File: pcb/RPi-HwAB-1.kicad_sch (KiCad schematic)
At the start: 5 parts, among them U1 CAT24C256

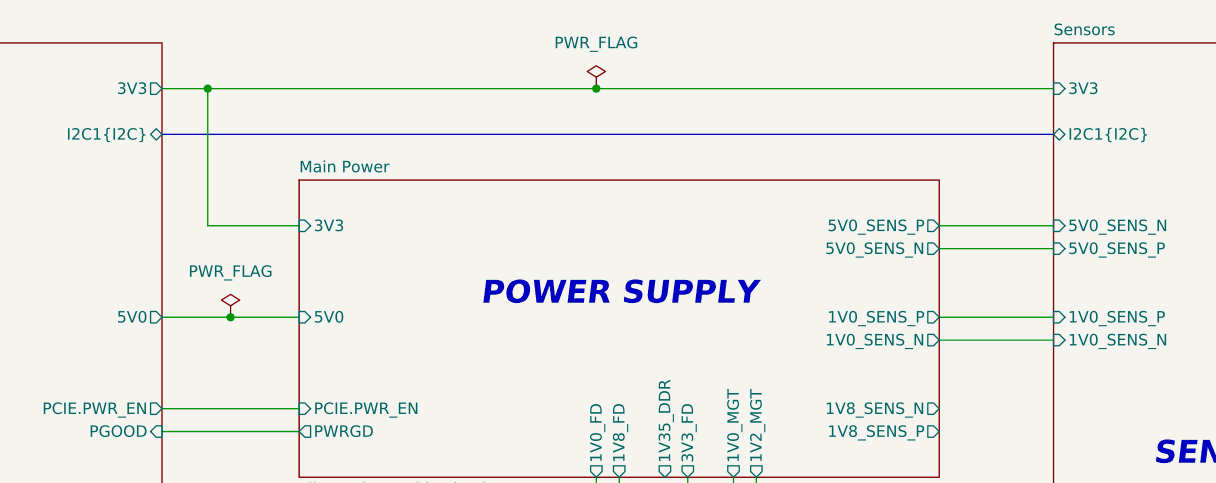
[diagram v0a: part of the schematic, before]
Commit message: moved stuff around, bom
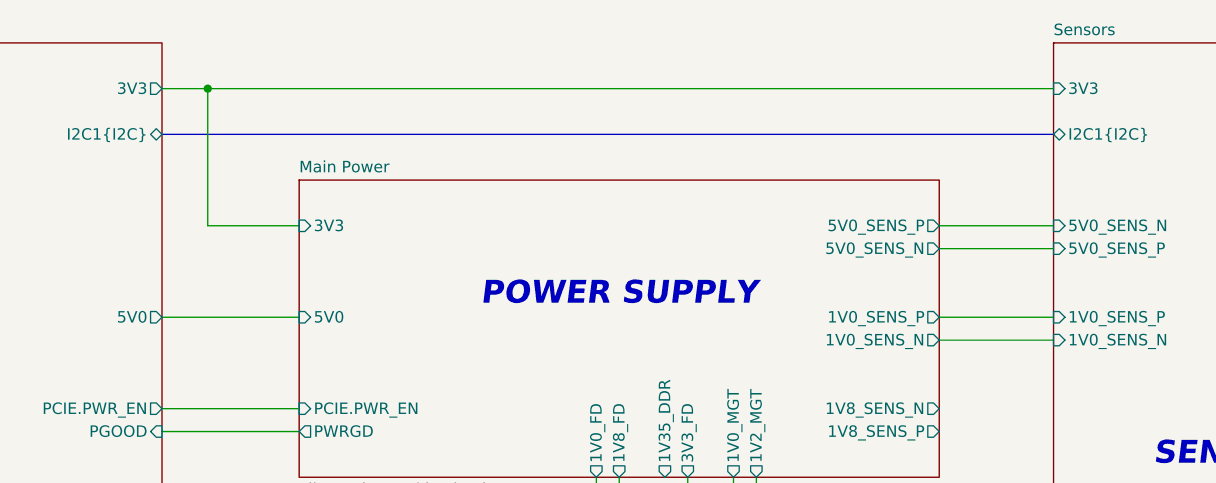
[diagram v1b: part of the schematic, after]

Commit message: jtag, dcplng
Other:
- sheet Connectors ports: added FPGA_PG; removed PGOOD
- sheet FPGA ports: added 1V35_DDR; removed none
- sheet Main Power ports: added 3V3_PG; removed PWRGD
- sheet Sensors ports: added 1V8_SENS_N, 1V8_SENS_P; removed none
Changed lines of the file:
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@@
 	(text "SENSORS"
 		(exclude_from_sim no)
-		(at 213.36 76.2 0)
+		(at 220.98 53.34 0)
 		(effects
 			(font
@@
 	)
 	(junction
-		(at 99.06 35.56)
+		(at 99.06 33.02)
 		(diameter 0)
-		(color 0 0 0 0)
+		(color 0 0 255 1)
 	)
 	(junction
@@
 	(wire
 		(pts
-			(xy 99.06 35.56) (xy 99.06 50.8)
+			(xy 99.06 33.02) (xy 99.06 50.8)
 		)
 		(stroke
@@
 	(bus
 		(pts
-			(xy 93.98 40.64) (xy 193.04 40.64)
+			(xy 93.98 38.1) (xy 193.04 38.1)
 		)
 		(stroke
@@
 	(wire
 		(pts
-			(xy 99.06 35.56) (xy 193.04 35.56)
+			(xy 99.06 33.02) (xy 193.04 33.02)
 		)
 		(stroke
@@
 	(wire
 		(pts
+			(xy 149.86 78.74) (xy 149.86 99.06)
+		)
+		(stroke
+			(width 0)
+			(type default)
+		)
+	)
+	(wire
+		(pts
 			(xy 101.6 173.99) (xy 101.6 177.8)
 		)
@@
 	(wire
 		(pts
+			(xy 180.34 73.66) (xy 193.04 73.66)
+		)
+		(stroke
+			(width 0)
+			(type default)
+		)
+	)
+	(wire
+		(pts
 			(xy 93.98 165.1) (xy 101.6 165.1)
 		)
@@
 	(wire
 		(pts
-			(xy 93.98 35.56) (xy 99.06 35.56)
+			(xy 93.98 33.02) (xy 99.06 33.02)
 		)
 		(stroke
@@
 		(pts
 			(xy 144.78 78.74) (xy 144.78 99.06)
+		)
+		(stroke
+			(width 0)
+			(type default)
+		)
+	)
+	(wire
+		(pts
+			(xy 180.34 71.12) (xy 193.04 71.12)
 		)
 		(stroke
@@
 	)
 	(sheet
-		(at 193.04 30.48)
-		(size 40.64 60.96)
+		(at 193.04 27.94)
+		(size 40.64 50.8)
 		(exclude_from_sim no)
 		(in_bom yes)
@@
 		)
 		(fill
-			(color 0 0 0 0.0000)
+			(color 0 0 72 0.0500)
 		)
 		(property "Sheetname" "Sensors"
-			(at 193.04 29.7684 0)
+			(at 193.04 27.2284 0)
 			(effects
 				(font
@@
 		)
 		(property "Sheetfile" "sensors.kicad_sch"
-			(at 193.04 92.0246 0)
+			(at 193.04 79.3246 0)
 			(effects
 				(font
@@
 		)
 		(pin "3V3" input
-			(at 193.04 35.56 180)
+			(at 193.04 33.02 180)
 			(effects
 				(font
@@
 		)
 		(pin "I2C1{I2C}" bidirectional
-			(at 193.04 40.64 180)
+			(at 193.04 38.1 180)
 			(effects
 				(font
@@
 		(pin "1V0_SENS_P" input
 			(at 193.04 60.96 180)
+			(effects
+				(font
+					(size 1.27 1.27)
+				)
+				(justify left)
+			)
+		)
+		(pin "1V8_SENS_N" input
+			(at 193.04 71.12 180)
+			(effects
+				(font
+					(size 1.27 1.27)
+				)
+				(justify left)
+			)
+		)
+		(pin "1V8_SENS_P" input
+			(at 193.04 73.66 180)
 			(effects
 				(font
@@
 	(sheet
 		(at 109.22 99.06)
-		(size 73.66 43.18)
+		(size 71.12 40.64)
 		(exclude_from_sim no)
 		(in_bom yes)
@@
 		)
 		(fill
-			(color 0 0 0 0.0000)
+			(color 0 72 72 0.0400)
 		)
 		(property "Sheetname" "FPGA"
@@
 		)
 		(property "Sheetfile" "fpga.kicad_sch"
-			(at 109.22 142.8246 0)
+			(at 109.22 140.2846 0)
 			(effects
 				(font
@@
 				)
 				(justify left)
+			)
+		)
+		(pin "1V35_DDR" input
+			(at 149.86 99.06 90)
+			(effects
+				(font
+					(size 1.27 1.27)
+				)
+				(justify right)
 			)
 		)
@@
 	)
 	(sheet
-		(at 58.42 30.48)
+		(at 58.42 27.94)
 		(size 35.56 111.76)
 		(exclude_from_sim no)
@@
 		)
 		(fill
-			(color 0 0 0 0.0000)
+			(color 72 0 72 0.0400)
 		)
 		(property "Sheetname" "Connectors"
-			(at 58.42 29.7684 0)
+			(at 58.42 27.2284 0)
 			(effects
 				(font
@@
 		)
 		(property "Sheetfile" "connectors.kicad_sch"
-			(at 58.42 142.8246 0)
+			(at 58.42 140.2846 0)
 			(effects
 				(font
@@
 		)
 		(pin "I2C1{I2C}" bidirectional
-			(at 93.98 40.64 0)
+			(at 93.98 38.1 0)
 			(effects
 				(font
@@
 		)
 		(pin "3V3" output
-			(at 93.98 35.56 0)
+			(at 93.98 33.02 0)
 			(effects
 				(font
@@
 			)
 		)
-		(pin "PGOOD" input
+		(pin "FPGA_PG" input
 			(at 93.98 73.66 0)
 			(effects
@@
 		)
 		(fill
-			(color 0 0 0 0.0000)
+			(color 72 0 0 0.0300)
 		)
 		(property "Sheetname" "Main Power"
@@
 			)
 		)
-		(pin "PWRGD" output
-			(at 109.22 73.66 180)
-			(effects
-				(font
-					(size 1.27 1.27)
-				)
-				(justify left)
-			)
-		)
 		(pin "5V0" input
 			(at 109.22 60.96 180)
@@
 			(effects
 				(font
+					(size 1.27 1.27)
+				)
+				(justify left)
+			)
+		)
+		(pin "3V3_PG" output
+			(at 109.22 73.66 180)
+			(effects
+				(font

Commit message: qspi
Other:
- sheet Connectors ports: added QSPI0{QSPI}; removed SPI0{SPI}
- sheet FPGA ports: added none; removed SPI0{SPI}
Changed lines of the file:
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@@
 	)
 	(bus_alias "SPI"
-		(members "MOSI" "MISO" "SCK" "CS0" "CS1")
+		(members "MOSI" "MISO" "SCLK" "CS0n" "CS1n")
 	)
 	(text "ARTIX 7 100T"
@@
 			)
 		)
-		(pin "SPI0{SPI}" bidirectional
-			(at 109.22 127 180)
-			(effects
-				(font
-					(size 1.27 1.27)
-				)
-				(justify left)
-			)
-		)
 		(pin "PCIE.RST_B" input
 			(at 109.22 109.22 180)
@@
 			)
 		)
-		(pin "SPI0{SPI}" bidirectional
-			(at 93.98 127 0)
-			(effects
-				(font
-					(size 1.27 1.27)
-				)
-				(justify right)
-			)
-		)
 		(pin "{JTAG}" bidirectional
 			(at 93.98 134.62 0)
@@
 			(effects
 				(font
+					(size 1.27 1.27)
+				)
+				(justify right)
+			)
+		)
+		(pin "QSPI0{QSPI}" bidirectional
+			(at 93.98 127 0)
+			(effects
+				(font

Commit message: quick fix top-level sch
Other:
- sheet FPGA ports: added QSPI0{QSPI}; removed none
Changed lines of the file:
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@@
+			)
+		)
+		(pin "QSPI0{QSPI}" bidirectional
+			(at 109.22 127 180)
+			(effects
+				(font
+					(size 1.27 1.27)
+				)
+				(justify left)
 			)
 		)

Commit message: bom
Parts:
- C1: value 100n -> 0.1uF; Manufacturer (none) -> KEMET; Manufacturer Product Number (none) -> C0402C104K4RACTU; Part Description (none) -> CAP CER 0.1UF 16V X7R 0402
- JP1: now left out of the parts list
- R1, R2: Manufacturer (none) -> YAGEO; Manufacturer Product Number (none) -> RC0402FR-073K9L; Part Description (none) -> RES 3.9K OHM 1% 1/16W 0402
- U1: footprint Package_DFN_QFN:DFN-8_2x2mm_P0.5mm -> Package_DFN_QFN:DFN-8-1EP_3x2mm_P0.5mm_EP1.7x1.4mm; Manufacturer (none) -> onsemi; Manufacturer Product Number (none) -> CAT24C256HU4IGT3; Part Description (none) -> IC EEPROM 256KBIT I2C 1MHZ 8UDFN
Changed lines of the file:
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@@
+			)
+		)
+		(property "Manufacturer" "YAGEO"
+			(at 93.98 170.18 0)
+			(effects
+				(font
+					(size 1.27 1.27)
+				)
+				(hide yes)
+			)
+		)
+		(property "Manufacturer Product Number" "RC0402FR-073K9L"
+			(at 93.98 170.18 0)
+			(effects
+				(font
+					(size 1.27 1.27)
+				)
+				(hide yes)
+			)
+		)
+		(property "Part Description" "RES 3.9K OHM 1% 1/16W 0402"
+			(at 93.98 170.18 0)
+			(effects
+				(font
+					(size 1.27 1.27)
+				)
+				(hide yes)
 			)
 		)
@@
 			)
 		)
-		(property "Value" "100n"
+		(property "Value" "0.1uF"
 			(at 64.9858 178.9493 0)
 			(effects
@@
 			)
 		)
+		(property "Manufacturer" "KEMET"
+			(at 67.31 177.8 0)
+			(effects
+				(font
+					(size 1.27 1.27)
+				)
+				(hide yes)
+			)
+		)
+		(property "Manufacturer Product Number" "C0402C104K4RACTU"
+			(at 67.31 177.8 0)
+			(effects
+				(font
+					(size 1.27 1.27)
+				)
+				(hide yes)
+			)
+		)
+		(property "Part Description" "CAP CER 0.1UF 16V X7R 0402"
+			(at 67.31 177.8 0)
+			(effects
+				(font
+					(size 1.27 1.27)
+				)
+				(hide yes)
+			)
+		)
 		(pin "1"
 		)
@@
 		(unit 1)
 		(exclude_from_sim no)
-		(in_bom yes)
+		(in_bom no)
 		(on_board yes)
 		(dnp no)
@@
 			)
 		)
+		(property "Name" ""
+			(at 96.52 180.34 0)
+			(effects
+				(font
+					(size 1.27 1.27)
+				)
+				(hide yes)
+			)
+		)
 		(pin "1"
 		)
@@
 			)
 		)
-		(property "Footprint" "Package_DFN_QFN:DFN-8_2x2mm_P0.5mm"
+		(property "Footprint" "Package_DFN_QFN:DFN-8-1EP_3x2mm_P0.5mm_EP1.7x1.4mm"
 			(at 81.28 177.8 0)
 			(effects
@@
 			)
 		)
+		(property "Manufacturer" "onsemi"
+			(at 81.28 177.8 0)
+			(effects
+				(font
+					(size 1.27 1.27)
+				)
+				(hide yes)
+			)
+		)
+		(property "Manufacturer Product Number" "CAT24C256HU4IGT3"
+			(at 81.28 177.8 0)
+			(effects
+				(font
+					(size 1.27 1.27)
+				)
+				(hide yes)
+			)
+		)
+		(property "Part Description" "IC EEPROM 256KBIT I2C 1MHZ 8UDFN"
+			(at 81.28 177.8 0)
+			(effects
+				(font
+					(size 1.27 1.27)
+				)
+				(hide yes)
+			)
+		)
 		(pin "1"
 		)
@@
 			(at 101.6 170.18 0)
 			(effects
+				(font
+					(size 1.27 1.27)
+				)
+				(hide yes)
+			)
+		)
+		(property "Manufacturer" "YAGEO"
+			(at 101.6 170.18 0)
+			(effects
+				(font
+					(size 1.27 1.27)
+				)
+				(hide yes)
+			)
+		)
+		(property "Manufacturer Product Number" "RC0402FR-073K9L"
+			(at 101.6 170.18 0)
+			(effects
+				(font
+					(size 1.27 1.27)
+				)
+				(hide yes)
+			)
+		)
+		(property "Part Description" "RES 3.9K OHM 1% 1/16W 0402"
+			(at 101.6 170.18 0)
+			(effects

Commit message: added mig ddr pinout constraints
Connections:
- net +3V3 renamed 3V3_RPi
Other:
- sheet Connectors ports: added 3V3_FD, 3V3_RPi; removed 3V3
- sheet Main Power ports: added none; removed 3V3
- sheet Sensors ports: added 3V3_RPi; removed 3V3

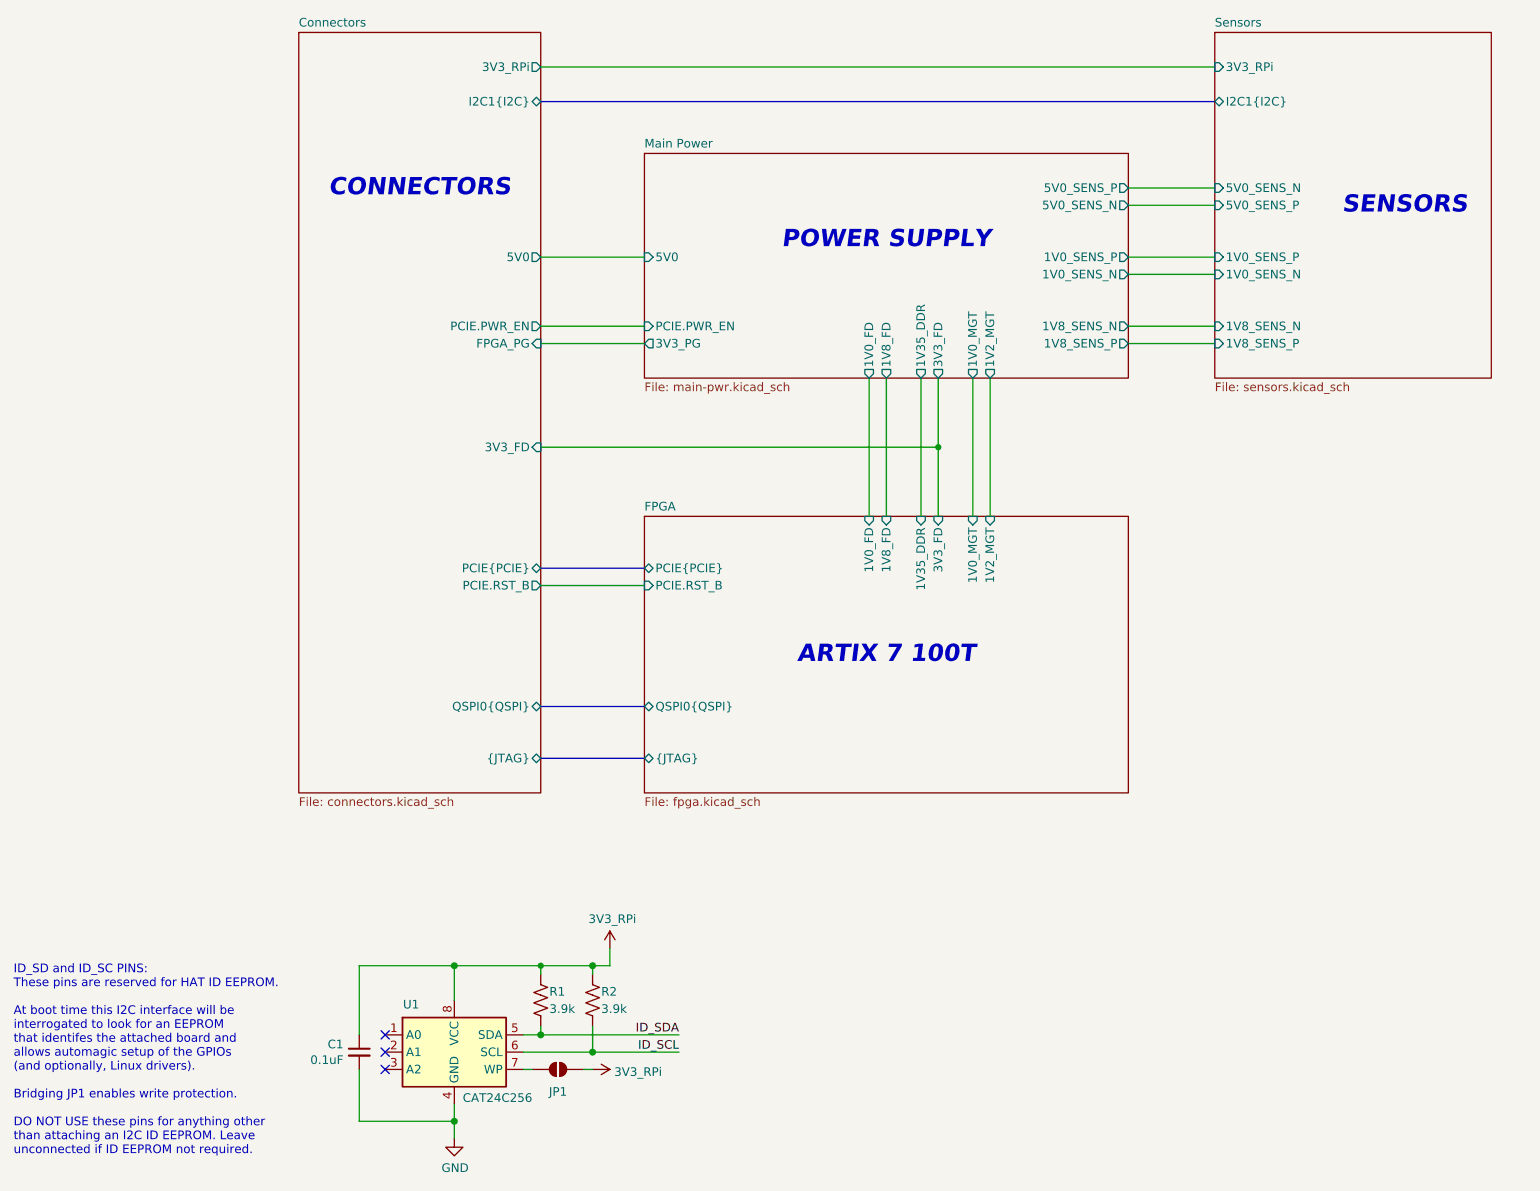
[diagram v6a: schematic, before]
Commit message: restructured power, power plane layout
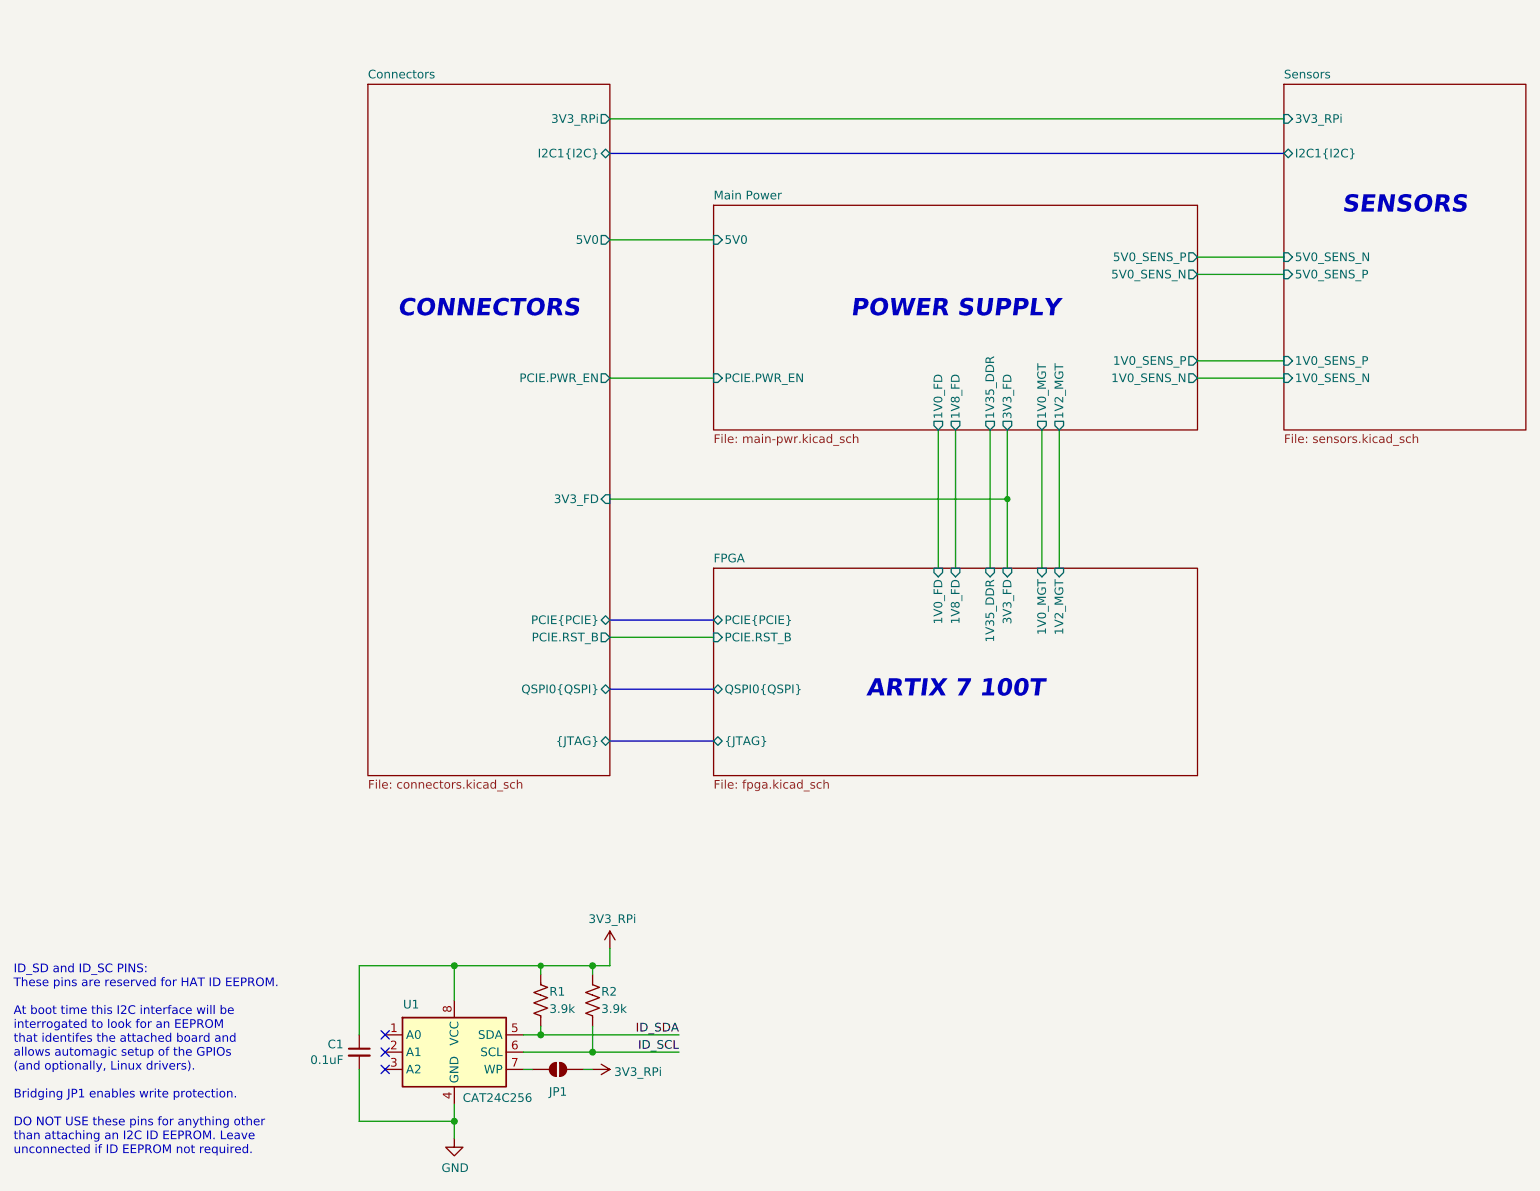
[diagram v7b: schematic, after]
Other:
- sheet Connectors ports: added none; removed FPGA_PG
- sheet Main Power ports: added none; removed 1V8_SENS_N, 1V8_SENS_P, 3V3_PG
- sheet Sensors ports: added none; removed 1V8_SENS_N, 1V8_SENS_P
